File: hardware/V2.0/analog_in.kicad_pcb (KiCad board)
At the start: 2 copper layers, 30 x 30 mm, 25 parts, among them J1 AKL_5_2, J2 AKL_5_2, P1 CON-SENSOR, U1 M24C64, U2 TLV272IS, U3 DRILL, U4 DRILL, U5 DRILL, U6 DRILL

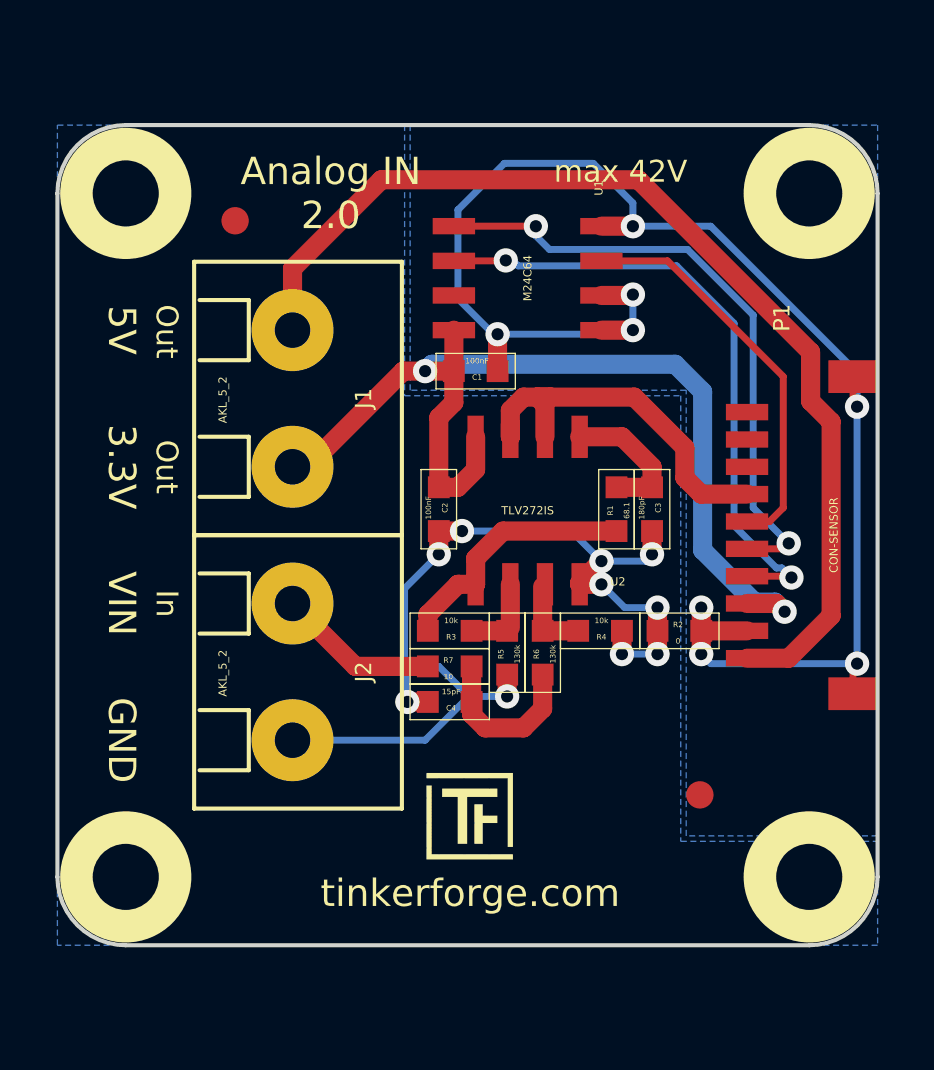
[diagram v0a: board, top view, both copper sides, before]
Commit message: changed to 5 connector design fuses added for voltage output
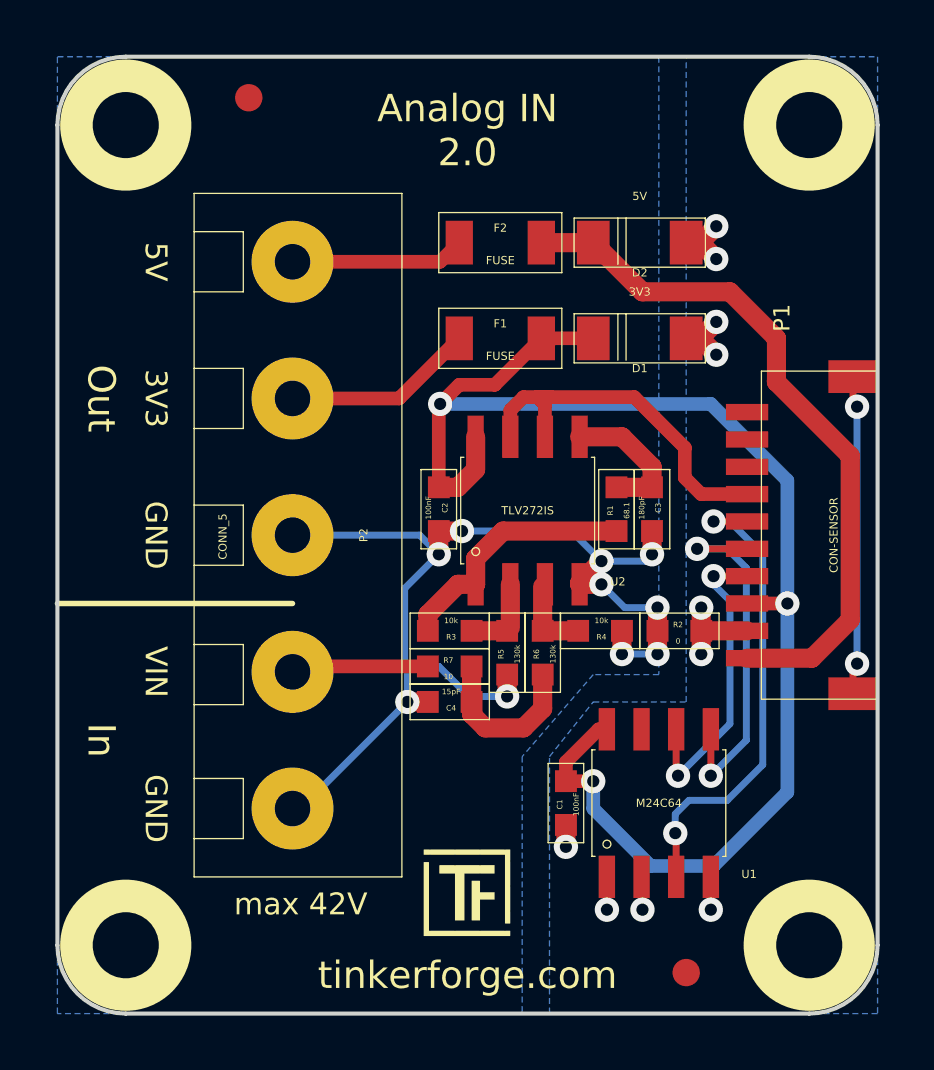
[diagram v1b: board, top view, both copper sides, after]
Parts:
- removed J1, J2: AKL_5_2, tinkerforge:AKL_5_2
- added D1: 3V3, kicad-libraries:MiniMelf, F.Cu at (196.8, 104.9)
- added D2: 5V, kicad-libraries:MiniMelf, F.Cu at (196.8, 101.4)
- added F1: FUSE, kicad-libraries:1206, F.Cu at (191.7, 104.9)
- added F2: FUSE, kicad-libraries:1206, F.Cu at (191.7, 101.4)
- added P2: CONN_5, kicad-libraries:AKL_5_5, F.Cu at (184.1, 112.1)
- C1, C2, C3, C4, R1, R2, R3, R4, R5, R6, R7: footprint tinkerforge:0603 -> kicad-libraries:0603
- P1: footprint tinkerforge:CON-SENSOR -> kicad-libraries:CON-SENSOR
- U1, U2: footprint tinkerforge:SOIC8 -> kicad-libraries:SOIC8
- U3, U4, U5, U6: footprint tinkerforge:DRILL_NP -> kicad-libraries:DRILL_NP
- moved U1 19.8 mm to (197.5, 121.9), turned to 0 degrees
- moved C1 16.1 mm to (194.1, 121.9), turned to 270 degrees
- moved Fiducial_Mark 6.52 mm to (198.5, 128.1)
- moved Fiducial_Mark 4.53 mm to (182.5, 96.1)
- moved G*** 2.80 mm to (188.9, 123.6)
- moved U3 2.50 mm to (178.0, 97.1)
- moved U4 2.50 mm to (178.0, 127.1)
- moved U5 2.50 mm to (203.0, 127.1)
- moved U6 2.50 mm to (203.0, 97.1)
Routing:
- net GND: track 57.5 -> 23.9 mm, vias 8 -> 12
- net 3V3: track 38.0 -> 53.0 mm, vias 2 -> 3
- net +5V: track 38.8 -> 25.8 mm
- net Net-(P1-Pad4): track 23.1 -> 11.3 mm
- net Net-(P1-Pad5): track 23.0 -> 14.4 mm
- net Net-(F1-Pad2): track 0.00 -> 7.01 mm
- net Net-(F2-Pad2): track 0.00 -> 6.39 mm
- net AGND: track 37.1 -> 41.5 mm
- net Net-(P1-Pad6): track 14.7 -> 17.5 mm, vias 0 -> 2
- net Net-(P2-Pad2): track 5.90 -> 5.03 mm
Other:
- board size 30 x 30 mm -> 30 x 35 mm
- board text added: "3V3"
- board text removed: "3.3V"
